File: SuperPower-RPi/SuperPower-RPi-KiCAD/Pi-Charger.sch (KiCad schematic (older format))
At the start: 12 parts, among them U2 BQ25895RTW

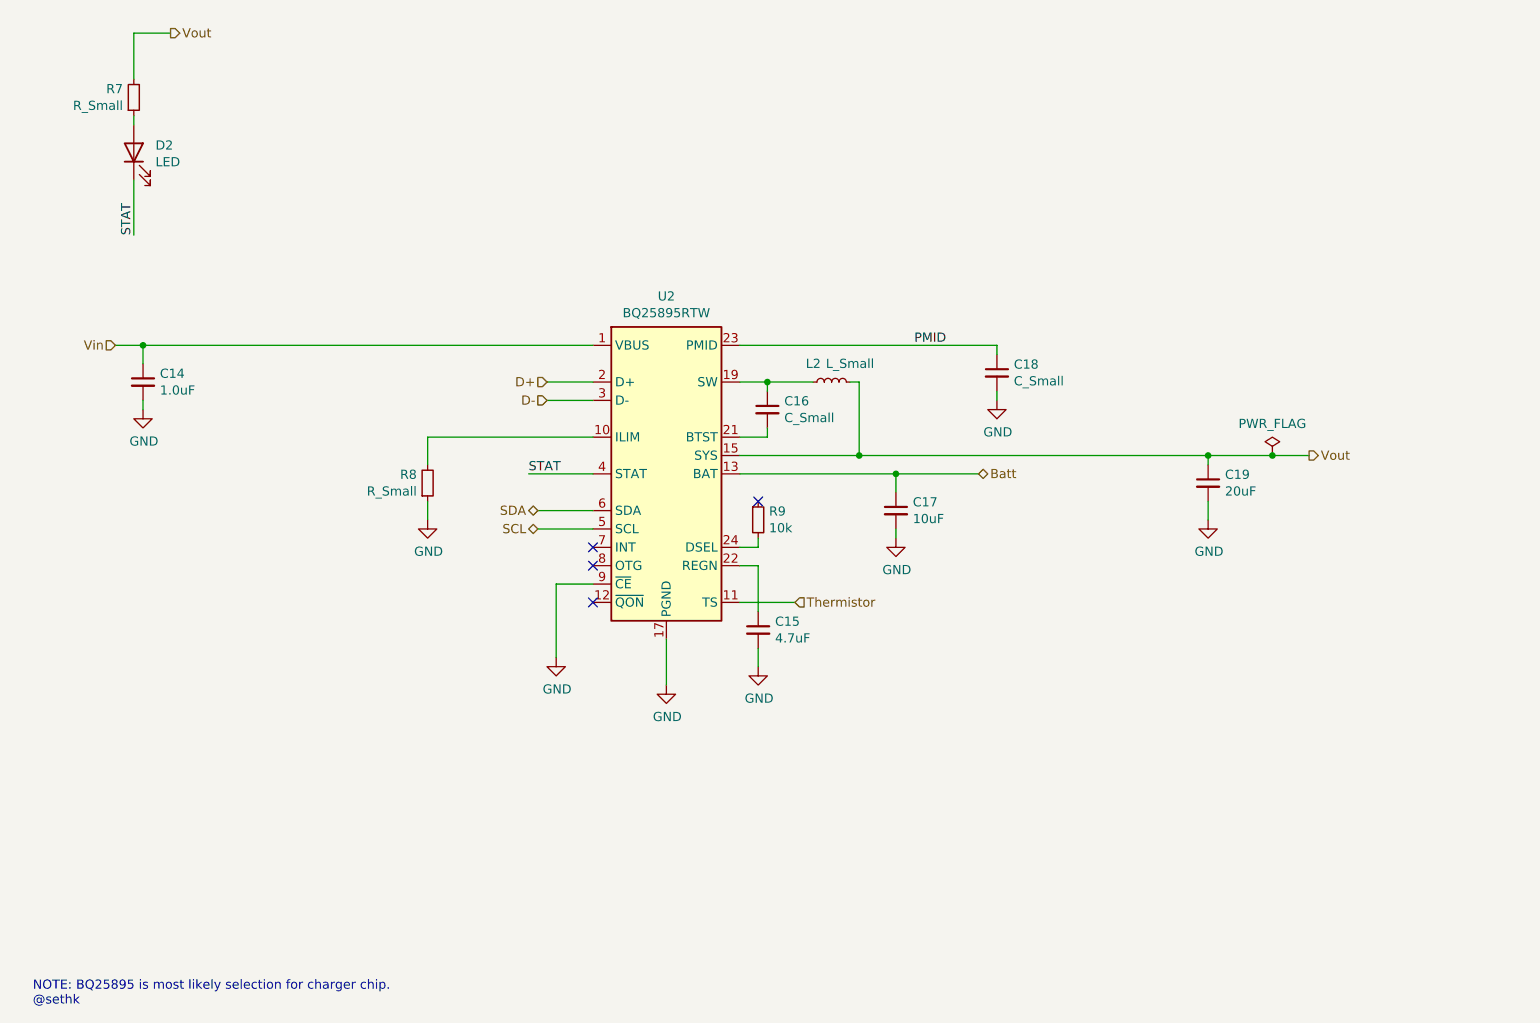
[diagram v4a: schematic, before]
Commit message: Filled out Charger IC surrounding component info.
(cherry picked from commit 3441b53fa3bafb5d00db46006ef3af0dc52ba3c8)
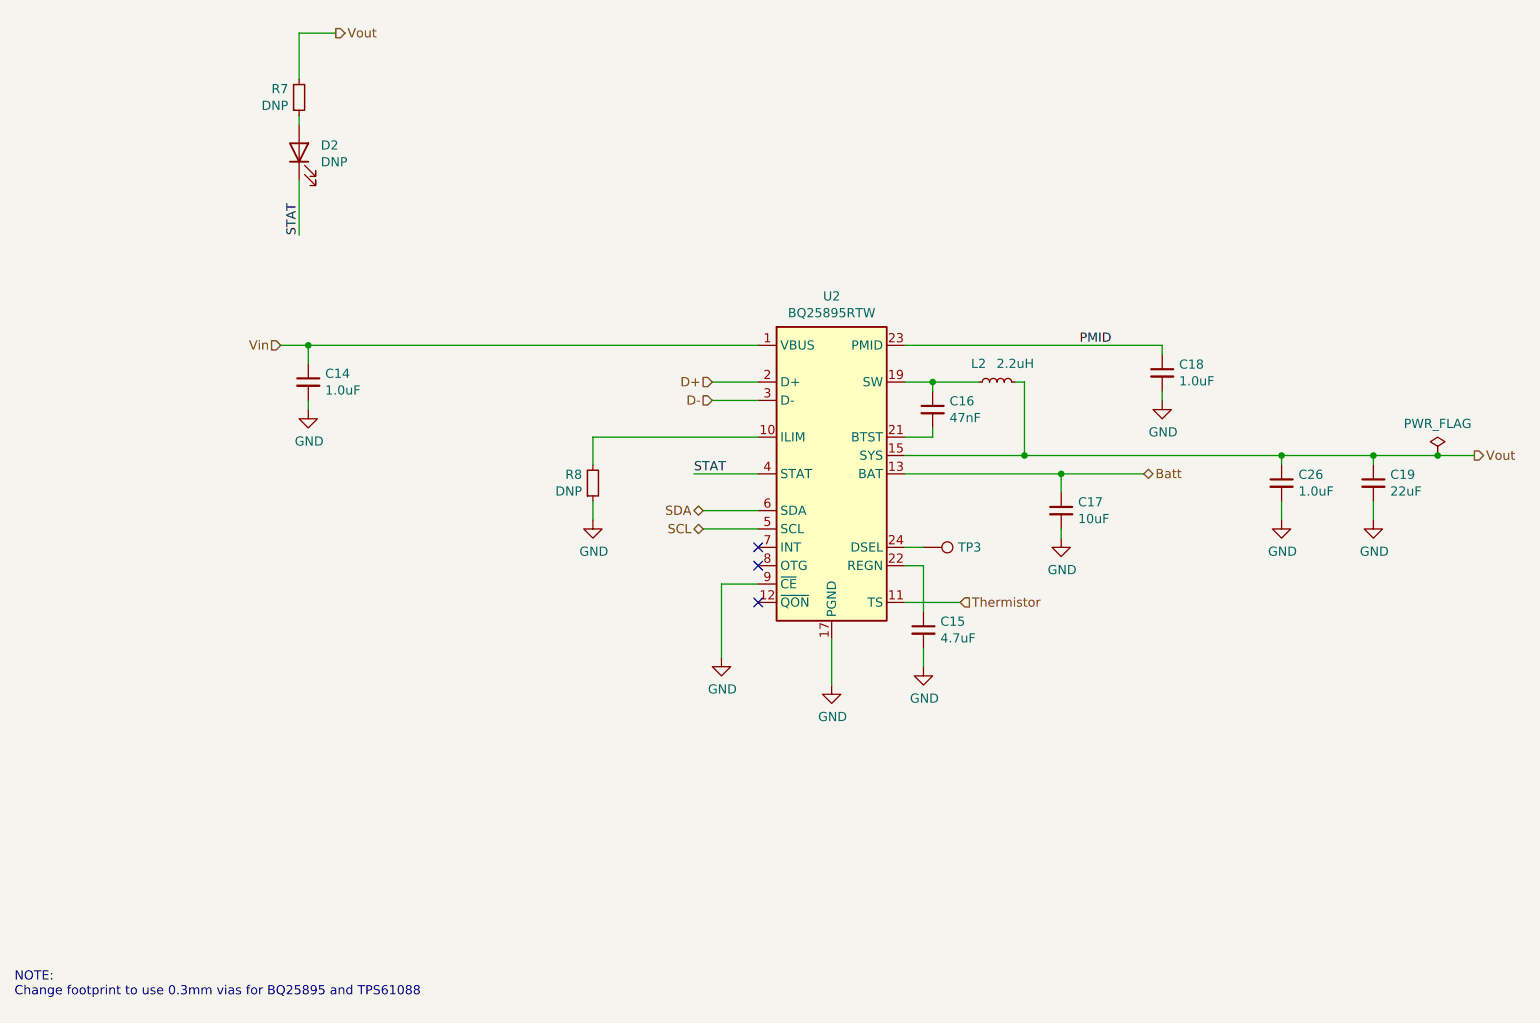
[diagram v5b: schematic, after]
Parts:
- removed R9: 10k, symbol Device:R_Small
- added C26: 1.0uF, Capacitor_SMD:C_0603_1608Metric, symbol Device:C_Small
- added TP3: DNP, TestPoint:TestPoint_Keystone_5000-5004_Miniature, symbol Connector:TestPoint
- C14: footprint (none) -> Capacitor_SMD:C_0603_1608Metric; Digi-Key PN (none) -> 1276-1184-1-ND; Mfg (none) -> Samsung; Mfg PN (none) -> CL10B105KA8NNNC
- C15: footprint (none) -> Capacitor_SMD:C_0603_1608Metric; Digi-Key PN (none) -> 1276-1900-1-ND; Mfg (none) -> Samsung; Mfg PN (none) -> CL10A475KA8NQNC
- C16: value C_Small -> 47nF; footprint (none) -> Capacitor_SMD:C_0603_1608Metric; Mfg (none) -> Yageo; Mfg PN (none) -> CC0603KRX7R9BB473
- C17: footprint (none) -> Capacitor_SMD:C_0805_2012Metric; Digi-Key PN (none) -> 490-5523-1-ND; Mfg (none) -> Murata; Mfg PN (none) -> CAP CER 10UF 25V X5R 0805
- C18: value C_Small -> 1.0uF; footprint (none) -> Capacitor_SMD:C_0603_1608Metric; Mfg (none) -> Samsung; Mfg PN (none) -> CL10B105KA8NNNC
- C19: value 20uF -> 22uF; footprint (none) -> Capacitor_SMD:C_1206_3216Metric; Digi-Key PN (none) -> 1276-3047-1-ND; Mfg (none) -> Samsung; Mfg PN (none) -> CL31A226KAHNNNE
- D2: value LED -> DNP; footprint (none) -> LED_SMD:LED_0603_1608Metric
- L2: value L_Small -> 2.2uH; footprint (none) -> Inductor_SMD:L_Vishay_IHLP-2525; Digi-Key PN (none) -> 541-1008-1-ND; Mfg (none) -> Vishay-Dale; Mfg PN (none) -> IHLP2525CZER2R2M01
- R7, R8: value R_Small -> DNP; footprint (none) -> Resistor_SMD:R_0603_1608Metric
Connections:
- net GND: now also C26.2
- net Vout: now also C26.1
- net at U2.24 (DSEL): now also TP3.1
- no-connect marks 4 -> 3
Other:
- note added: "NOTE:\nChange footprint to use 0.3mm vias for BQ25895 and TPS61088"
- note removed: "NOTE: BQ25895 is most likely selection for charger chip.\n@sethk"
- moved on the sheet: C14, C15, C16, C17, C18, C19, D2, L2, R7, R8, U2

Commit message: Updated components. Mostly caps and resistors.
(cherry picked from commit e921c80666429be92cc496d87bcbd557350196b5)
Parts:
- C17: Mfg PN CAP CER 10UF 25V X5R 0805 -> GRM21BR61E106KA73L
- C18, C26: Digi-Key PN (none) -> 1276-1184-1-ND
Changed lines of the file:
@@
 F 3 "~" H 6900 3950 50  0001 C CNN
 F 4 "Murata" H 6900 3950 50  0001 C CNN "Mfg"
-F 5 "CAP CER 10UF 25V X5R 0805" H 6900 3950 50  0001 C CNN "Mfg PN"
+F 5 "GRM21BR61E106KA73L" H 6900 3950 50  0001 C CNN "Mfg PN"
 F 6 "490-5523-1-ND" H 6900 3950 50  0001 C CNN "Digi-Key PN"
 	1    6900 3950
@@
 F 4 "Samsung" H 7450 3200 50  0001 C CNN "Mfg"
 F 5 "CL10B105KA8NNNC" H 7450 3200 50  0001 C CNN "Mfg PN"
+F 6 "1276-1184-1-ND" H 7450 3200 50  0001 C CNN "Digi-Key PN"
 	1    7450 3200
 	1    0    0    -1
@@
 F 4 "Samsung" H 8100 3800 50  0001 C CNN "Mfg"
 F 5 "CL10B105KA8NNNC" H 8100 3800 50  0001 C CNN "Mfg PN"
+F 6 "1276-1184-1-ND" H 8100 3800 50  0001 C CNN "Digi-Key PN"
 	1    8100 3800
 	1    0    0    -1

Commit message: Part Meta-data updates continued.
(cherry picked from commit d0ad2c93dfb1e315a7dc98683a53ed7dcb5f49ff)
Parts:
- U2: Digi-Key PN (none) -> 296-44345-1-ND; Mfg (none) -> Texas Instruments; Mfg PN (none) -> BQ25895RTWR
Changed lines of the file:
@@
 F 2 "Package_DFN_QFN:Texas_S-PWQFN-N24_EP2.7x2.7mm_ThermalVias" H 5550 4750 50  0001 C CNN
 F 3 "http://www.ti.com/lit/ds/symlink/bq25895.pdf" H 5450 4550 50  0001 C CNN
+F 4 "296-44345-1-ND" H 5650 3750 50  0001 C CNN "Digi-Key PN"
+F 5 "Texas Instruments" H 5650 3750 50  0001 C CNN "Mfg"
+F 6 "BQ25895RTWR" H 5650 3750 50  0001 C CNN "Mfg PN"
 	1    5650 3750
 	1    0    0    -1

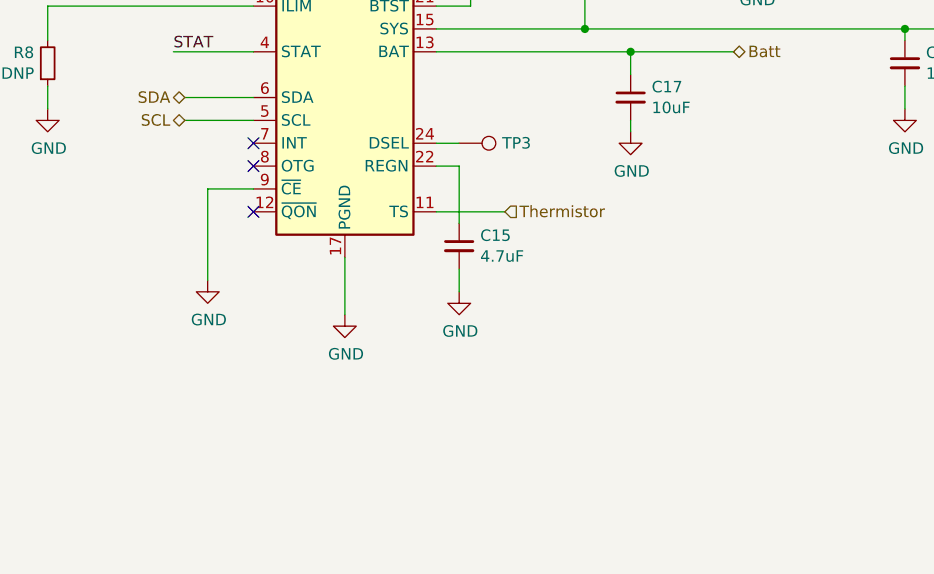
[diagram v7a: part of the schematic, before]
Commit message: Added Thermistor voltage divider and jumper on CE.
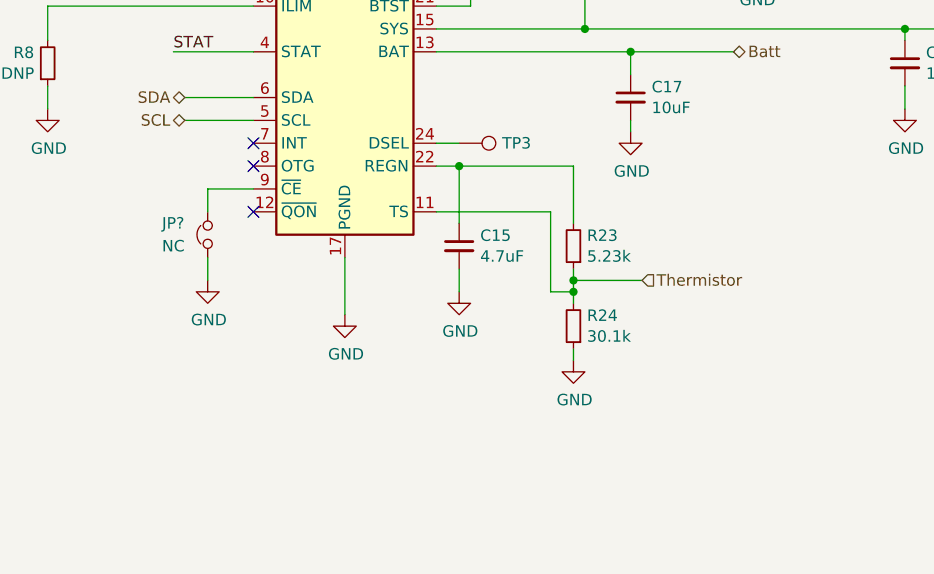
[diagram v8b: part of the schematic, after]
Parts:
- added JP?: NC, Jumper:SolderJumper-2_P1.3mm_Bridged_Pad1.0x1.5mm, symbol Device:Jumper_NC_Small
- added R23: 5.23k, Resistor_SMD:R_0603_1608Metric, symbol Device:R_Small
- added R24: 30.1k, Resistor_SMD:R_0603_1608Metric, symbol Device:R_Small
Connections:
- net GND: now also JP?.1, R24.1; no longer U2.9 (~CE)
- net Thermistor: now also R23.1, R24.2
- net at C15.1, U2.22 (REGN): now also R23.2
- new net: JP?.2, U2.9 (~CE)
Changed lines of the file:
@@
 $Descr A4 11693 8268
 encoding utf-8
-Sheet 8 8
+Sheet 7 8
 Title ""
 Date ""
@@
 $EndComp
 Wire Wire Line
-	5050 4750 5050 4350
-Wire Wire Line
 	5050 4350 5250 4350
 $Comp
@@
 Wire Wire Line
 	2800 3050 5250 3050
-Wire Wire Line
-	6050 4450 6350 4450
-Text HLabel 6350 4450 2    50   Input ~ 0
+Text HLabel 6950 4750 2    50   Input ~ 0
 Thermistor
 $Comp
@@
 Wire Wire Line
 	8100 4000 8100 3900
+$Comp
+L Device:R_Small R23
+U 1 1 5FBA68CC
+P 6650 4600
+F 0 "R23" H 6591 4554 50  0000 R CNN
+F 1 "5.23k" H 6591 4645 50  0000 R CNN
+F 2 "Resistor_SMD:R_0603_1608Metric" H 6650 4600 50  0001 C CNN
+F 3 "~" H 6650 4600 50  0001 C CNN
+	1    6650 4600
+	-1   0    0    1
+$EndComp
+$Comp
+L Device:R_Small R24
+U 1 1 5FBA6D8C
+P 6650 4950
+F 0 "R24" H 6591 4904 50  0000 R CNN
+F 1 "30.1k" H 6591 4995 50  0000 R CNN
+F 2 "Resistor_SMD:R_0603_1608Metric" H 6650 4950 50  0001 C CNN
+F 3 "~" H 6650 4950 50  0001 C CNN
+	1    6650 4950
+	-1   0    0    1
+$EndComp
+Wire Wire Line
+	6650 4750 6950 4750
+Wire Wire Line
+	6650 4500 6650 4250
+Connection ~ 6150 4250
+Wire Wire Line
+	6150 4250 6650 4250
+Connection ~ 6650 4750
+Wire Wire Line
+	6650 4750 6650 4700
+Wire Wire Line
+	6650 4750 6650 4800
+Wire Wire Line
+	6650 4800 6550 4800
+Wire Wire Line
+	6550 4800 6550 4450
+Wire Wire Line
+	6550 4450 6050 4450
+Connection ~ 6650 4800
+Wire Wire Line
+	6650 4800 6650 4850
+$Comp
+L power:GND #PWR039
+U 1 1 5FBB2617
+P 6650 5100
+F 0 "#PWR039" H 6650 4850 50  0001 C CNN
+F 1 "GND" H 6655 4927 50  0000 C CNN
+F 2 "" H 6650 5100 50  0001 C CNN
+F 3 "" H 6650 5100 50  0001 C CNN
+	1    6650 5100
+	1    0    0    -1
+$EndComp
+Wire Wire Line
+	6650 5100 6650 5050
+$Comp
+L Device:Jumper_NC_Small JP?
+U 1 1 5FBBB98D
+P 5050 4550
+F 0 "JP?" V 5100 4750 50  0000 R CNN
+F 1 "NC" V 5000 4750 50  0000 R CNN
+F 2 "Jumper:SolderJumper-2_P1.3mm_Bridged_Pad1.0x1.5mm" H 5050 4550 50  0001 C CNN
+F 3 "~" H 5050 4550 50  0001 C CNN
+	1    5050 4550
+	0    -1   -1   0
+$EndComp
+Wire Wire Line
+	5050 4450 5050 4350
+Wire Wire Line
+	5050 4650 5050 4750
 $EndSCHEMATC
